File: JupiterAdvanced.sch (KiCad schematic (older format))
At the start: 21 parts

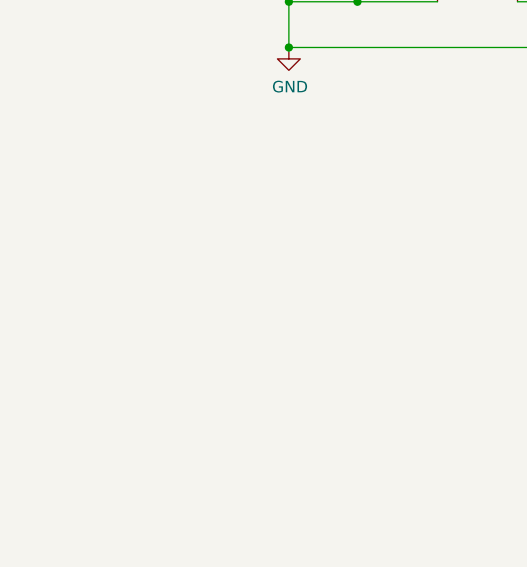
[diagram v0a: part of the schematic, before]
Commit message: Key Switch Matrix added
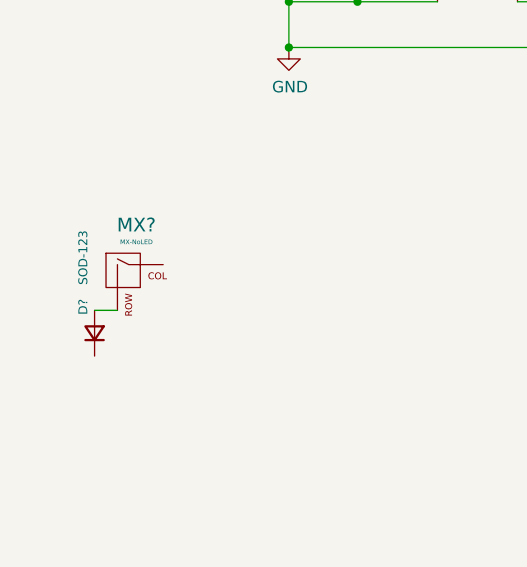
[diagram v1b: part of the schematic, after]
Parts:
- added D?: SOD-123, symbol Device:D_Small
- added MX?: MX-NoLED, symbol MX_Alps_Hybrid:MX-NoLED
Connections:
- new net: D?.2 (A), MX?.2 (ROW)
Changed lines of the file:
@@
 Wire Wire Line
 	2750 2450 2900 2450
+$Comp
+L MX_Alps_Hybrid:MX-NoLED MX?
+U 1 1 607C74DD
+P 1050 3650
+F 0 "MX?" H 1083 3873 60  0000 C CNN
+F 1 "MX-NoLED" H 1083 3799 20  0000 C CNN
+F 2 "" H 425 3625 60  0001 C CNN
+F 3 "" H 425 3625 60  0001 C CNN
+	1    1050 3650
+	1    0    0    -1
+$EndComp
+$Comp
+L Device:D_Small D?
+U 1 1 607C81EE
+P 900 3900
+F 0 "D?" H 1050 3950 39  0000 R CNN
+F 1 "SOD-123" H 1350 3950 39  0000 R CNN
+F 2 "" V 900 3900 50  0001 C CNN
+F 3 "~" V 900 3900 50  0001 C CNN
+	1    900  3900
+	0    -1   -1   0
+$EndComp
+Wire Wire Line
+	1000 3800 900  3800
 $EndSCHEMATC

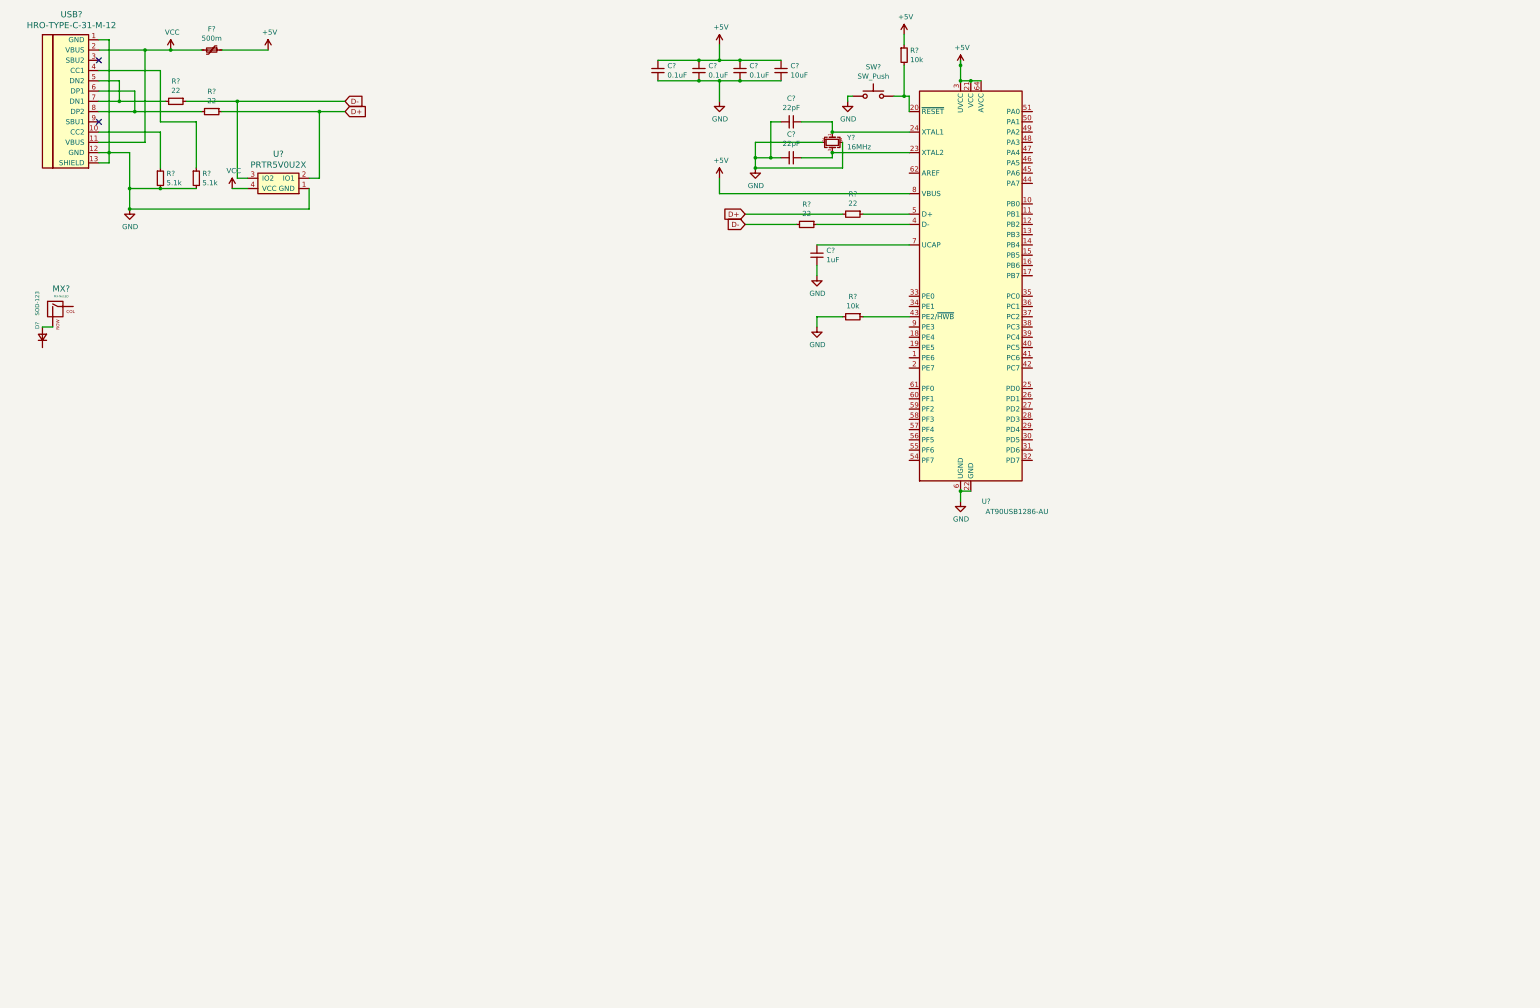
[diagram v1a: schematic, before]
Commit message: Key Switch Matrix completed
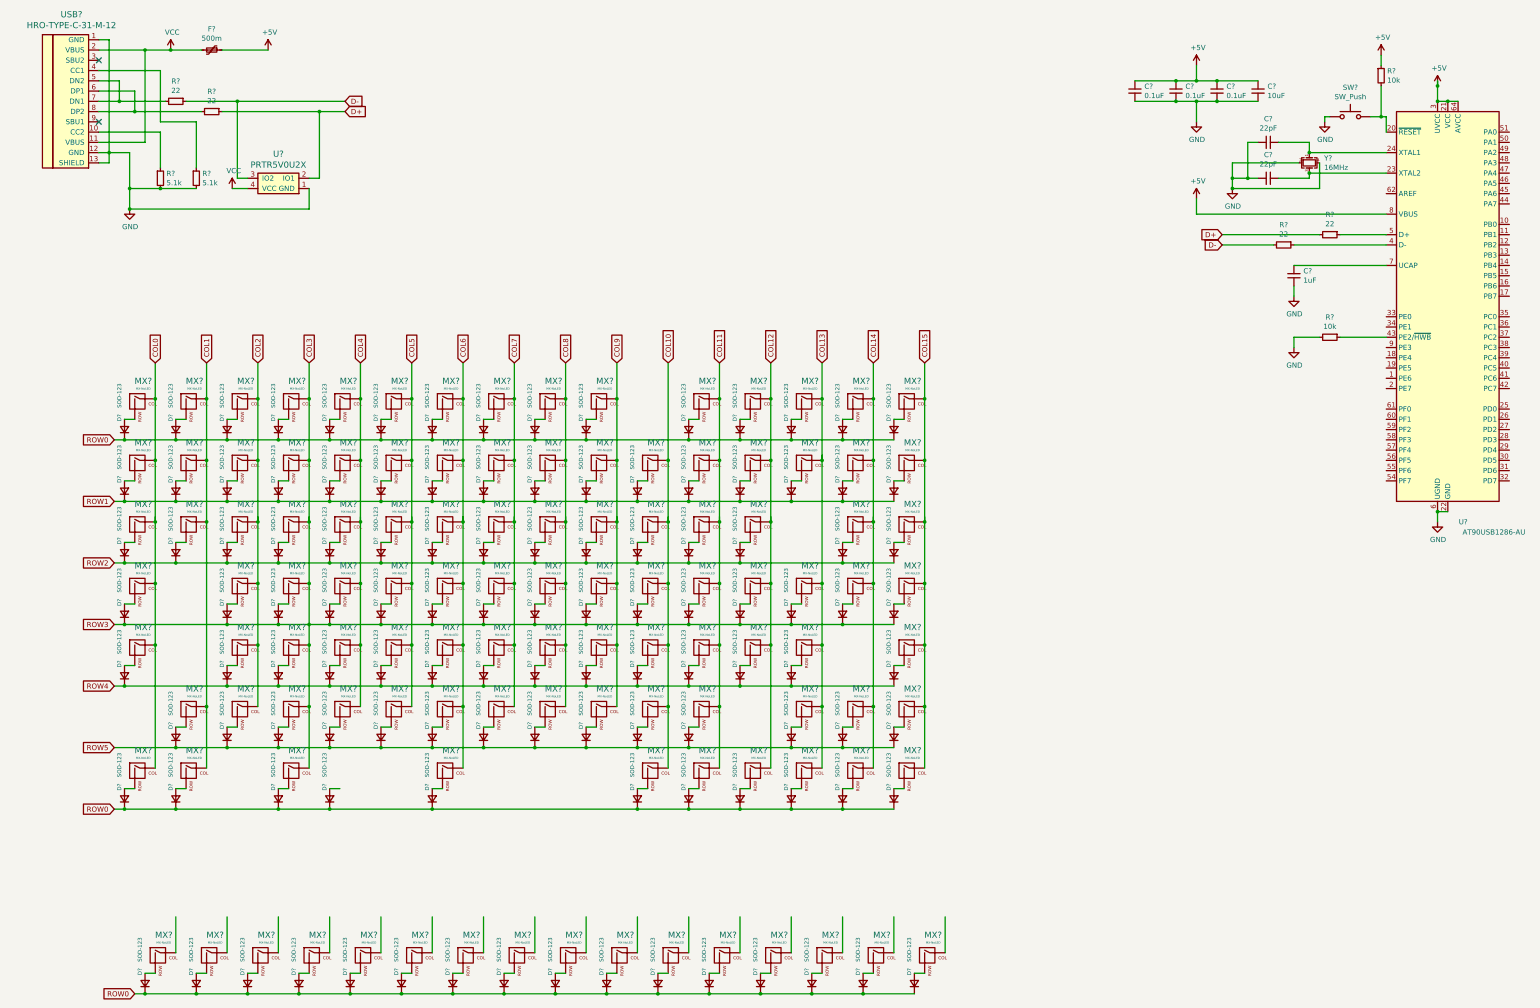
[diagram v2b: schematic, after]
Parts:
- added D? (x115): SOD-123, symbol Device:D_Small
- added MX? (x114): MX-NoLED, symbol MX_Alps_Hybrid:MX-NoLED
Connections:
- net labels added: COL0, COL1, COL10, COL11, COL12, COL13, COL14, COL15, COL2, COL3, COL4, COL5, COL6, COL7, COL8, COL9, ROW0, ROW1, ROW2, ROW3, ROW4, ROW5
- wire segments 91 -> 454
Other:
- moved on the sheet: C?, D?, MX?, R?, SW?, U?, Y?

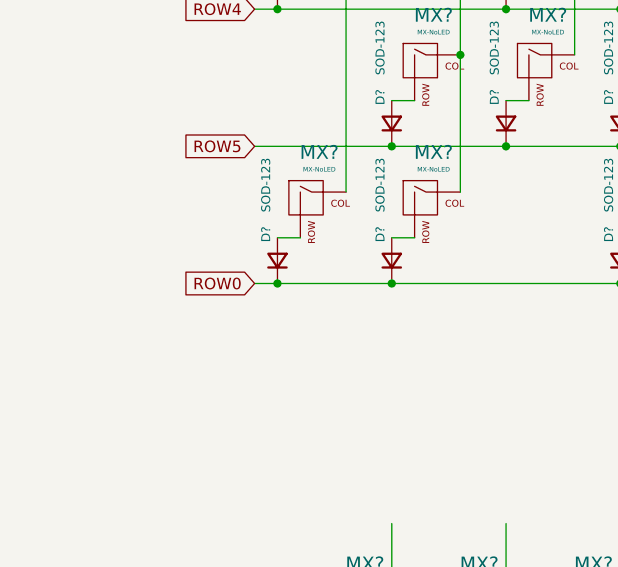
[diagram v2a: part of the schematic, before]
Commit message: Key Switch Matrix Row numbering fixed
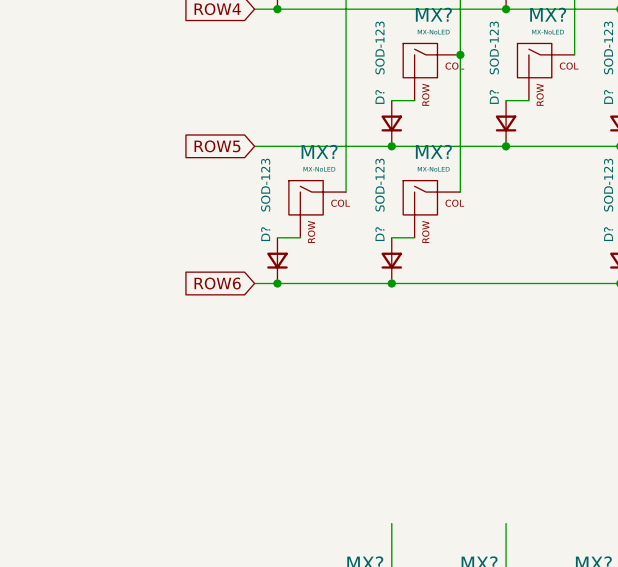
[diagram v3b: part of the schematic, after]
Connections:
- net labels added: ROW6
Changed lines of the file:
@@
 	8800 8300 8700 8300
 Text GLabel 1600 8500 0    50   Input ~ 0
-ROW0
+ROW6
 Wire Wire Line
 	1600 8500 1700 8500

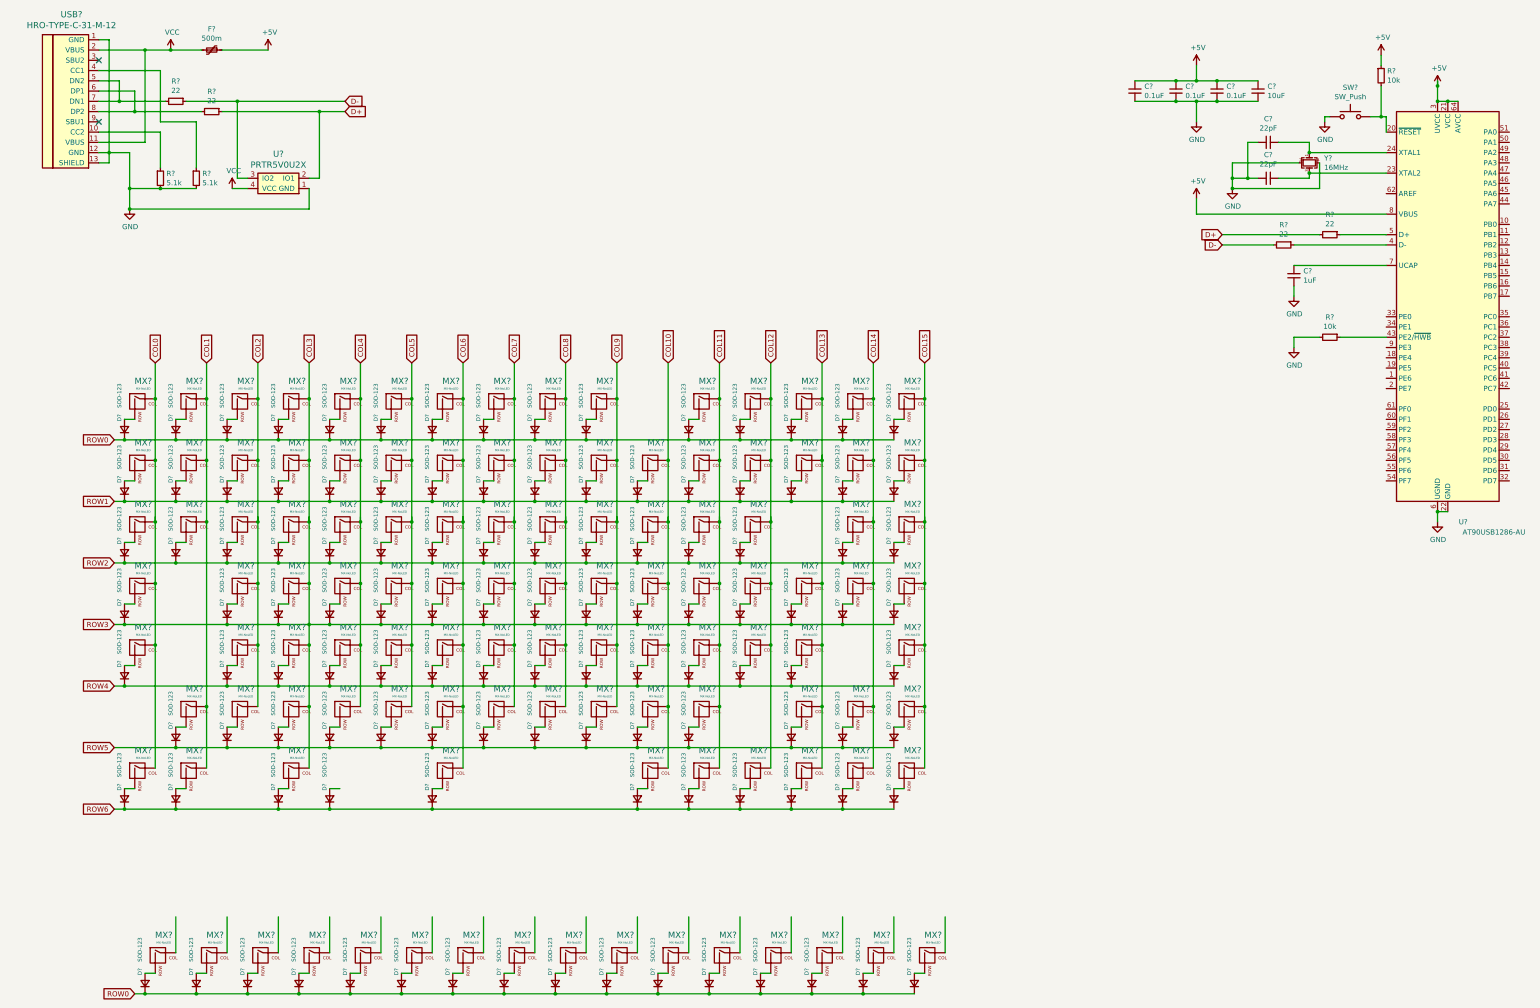
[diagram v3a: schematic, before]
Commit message: Key Switch labeling complete
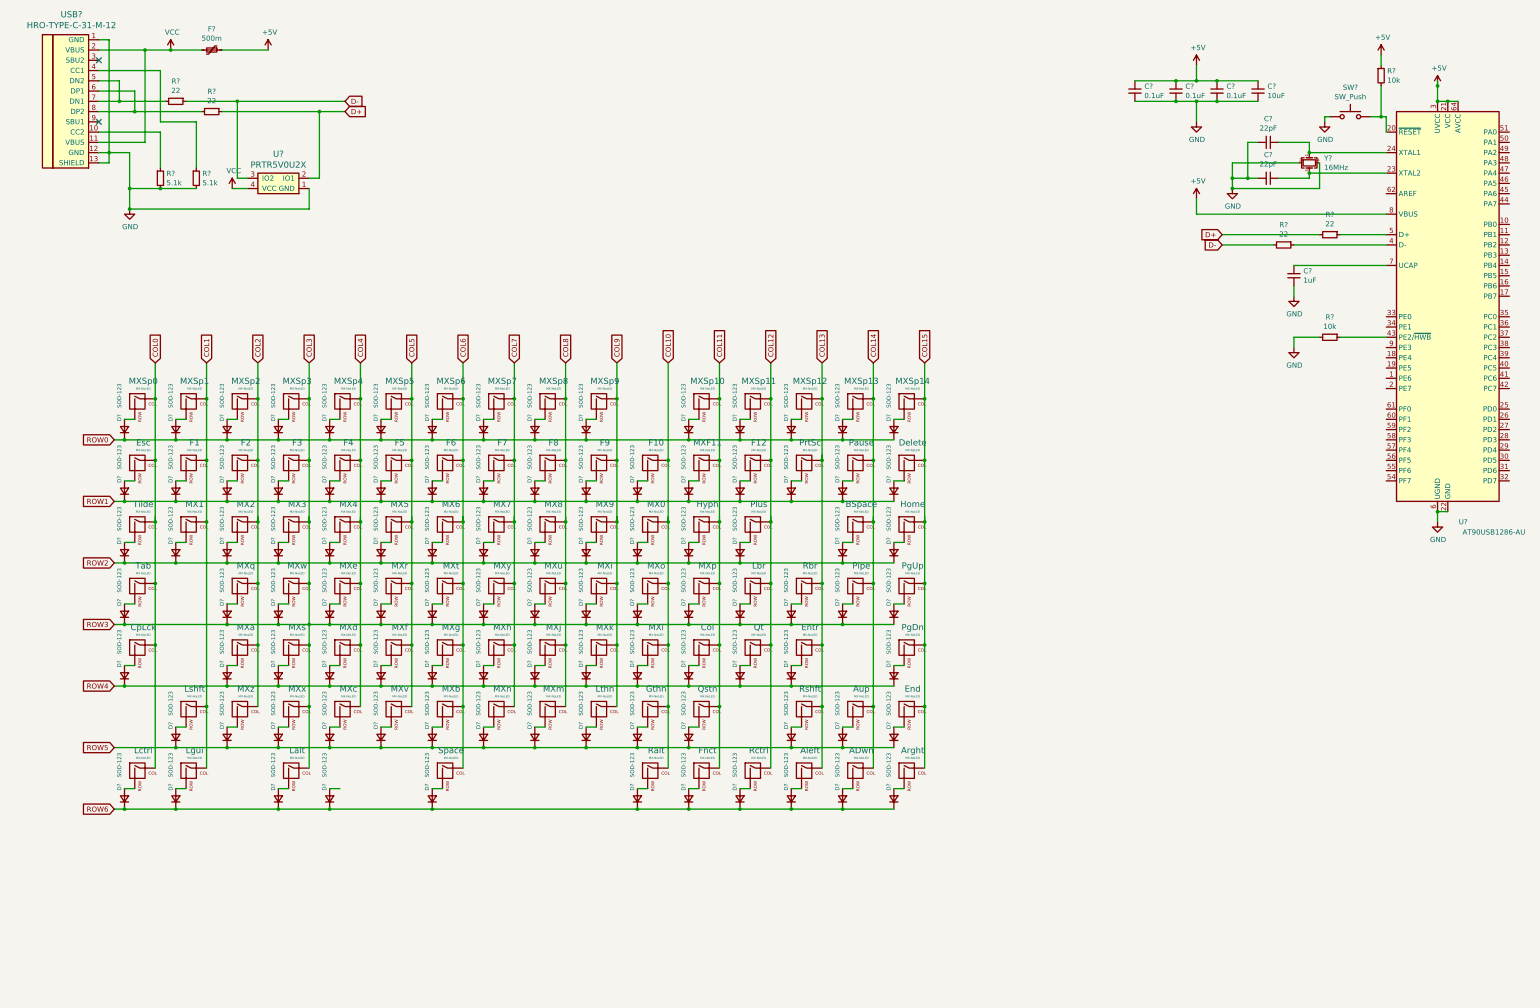
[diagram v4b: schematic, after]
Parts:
- removed D? (x16): SOD-123, symbol Device:D_Small
- removed MX? (x16): MX-NoLED, symbol MX_Alps_Hybrid:MX-NoLED
- gave numbers to parts that had none: 99
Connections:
- wire segments 454 -> 406
